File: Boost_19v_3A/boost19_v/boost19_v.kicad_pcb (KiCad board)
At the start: 2 copper layers, 20 parts, among them J1 4P2C, J2 4P2C, U1 TPS55340QRTERQ1

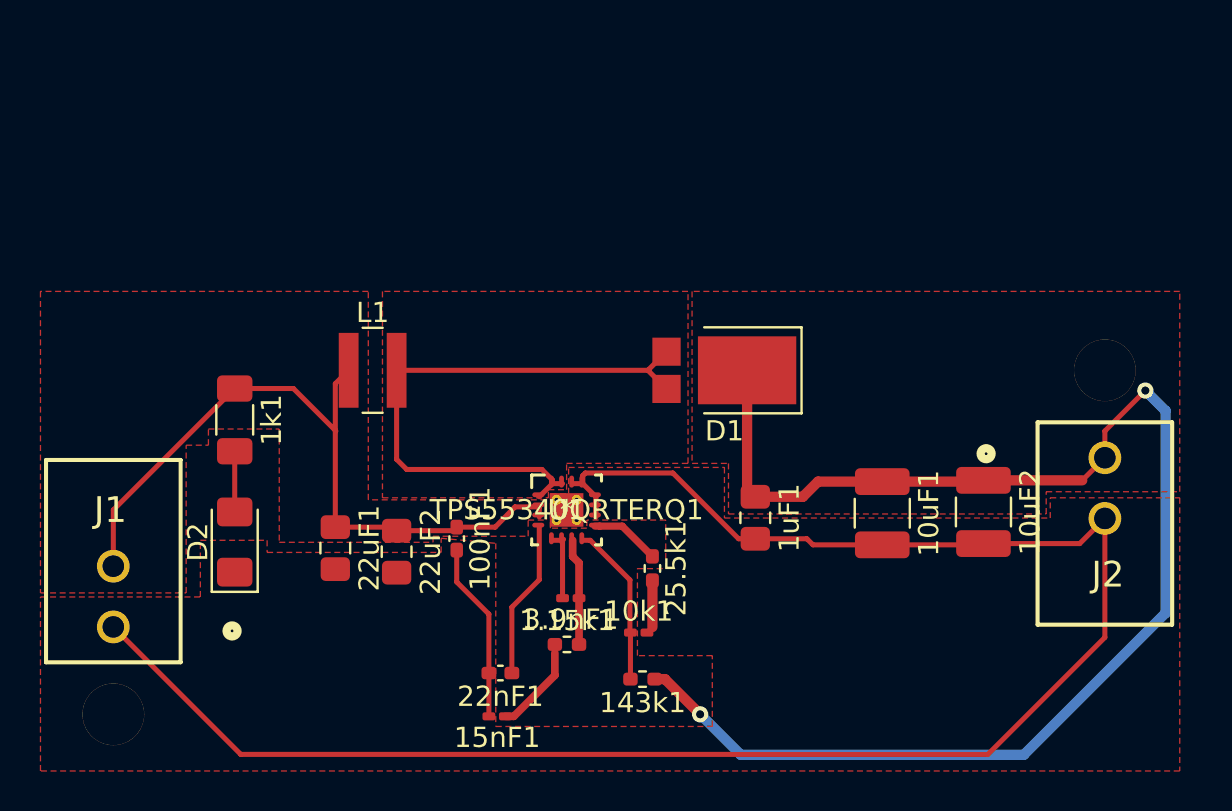
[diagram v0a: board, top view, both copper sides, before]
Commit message: boost19v pcb layout updated
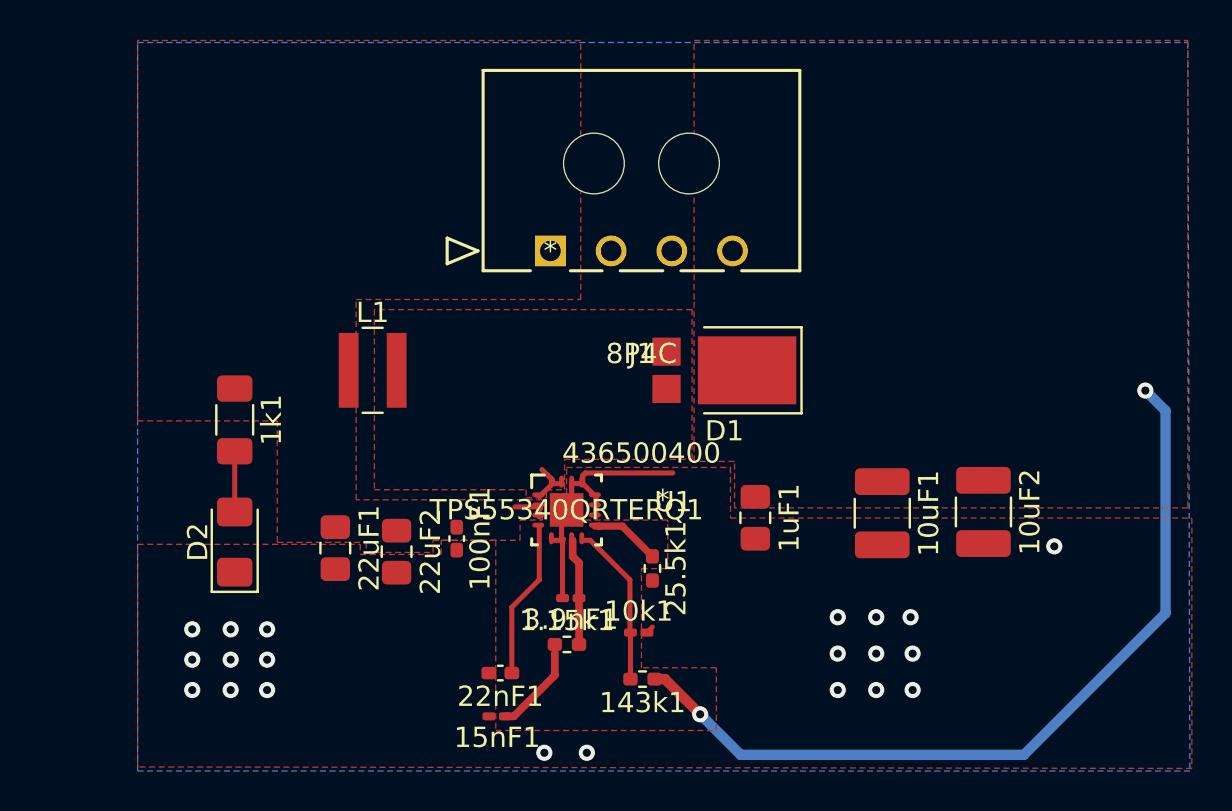
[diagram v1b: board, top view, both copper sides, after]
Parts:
- removed J2: 4P2C, 4p2c:43045-0200
- J1: value 4P2C -> 8P4C; footprint 4p2c:43045-0200 -> 4x1_connector:436500400
- U1: footprint IC:TPS55340QRTERQ1 -> IC_update:TPS55340QRTERQ1_002
- moved J1 31.5 mm to (131.6, 84.1), turned to 180 degrees
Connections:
- 100nF1 pad 2: GND -> Net-(100nF1-Pad2)
- 10k1 pad 2: GND -> Net-(100nF1-Pad2)
- 10uF1 pad 2: GND -> Net-(100nF1-Pad2)
- 10uF2 pad 2: GND -> Net-(100nF1-Pad2)
- 15nF1 pad 2: GND -> Net-(100nF1-Pad2)
- 1uF1 pad 2: GND -> Net-(100nF1-Pad2)
- 22nF1 pad 2: GND -> Net-(100nF1-Pad2)
- 22uF1 pad 2: GND -> Net-(100nF1-Pad2)
- 22uF2 pad 2: GND -> Net-(100nF1-Pad2)
- 25.5k1 pad 2: GND -> Net-(100nF1-Pad2)
- 3.9nF1 pad 2: GND -> Net-(100nF1-Pad2)
- D2 pad 1: GND -> Net-(100nF1-Pad2)
- J1 pad 1: GND -> Net-(100nF1-Pad1)
- J1 pad 2: Net-(100nF1-Pad1) -> Net-(100nF1-Pad2)
- J1 pad 3: (no net) -> Net-(100nF1-Pad2)
- U1 pad 10: GND -> Net-(100nF1-Pad2)
- U1 pad 11: GND -> Net-(100nF1-Pad2)
- U1 pad 12: GND -> Net-(100nF1-Pad2)
- U1 pad 13: GND -> Net-(100nF1-Pad2)
- U1 pad 14: GND -> Net-(100nF1-Pad2)
- U1 pad 17: GND -> Net-(100nF1-Pad2)
- U1 pad 5: GND -> Net-(100nF1-Pad2)
- U1 pad 6: GND -> Net-(100nF1-Pad2)
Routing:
- net GND: track 106.0 -> 0.00 mm
- net Net-(100nF1-Pad1): track 36.3 -> 1.70 mm
- net Net-(10uF1-Pad1): track 69.8 -> 41.1 mm
- net Net-(D1-Pad2): track 29.1 -> 2.33 mm
- net Net-(100nF1-Pad2): track 0.00 -> 14.2 mm, vias 0 -> 21
- added copper zone on B.Cu, net Net-(100nF1-Pad2)
- added copper zone on F.Cu, net Net-(100nF1-Pad2)
- removed copper zone on F.Cu, net GND
